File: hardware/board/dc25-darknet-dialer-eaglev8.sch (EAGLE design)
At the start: 86 parts, among them SW1 RESET, X1 10118193-0001LF, Y1 RESONATORSMD

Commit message: Updated silk screen parts indicators
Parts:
- renumbered SAMPLE_CAP_G1 to C23, SAMPLE_CAP_G2 to C24, SAMPLE_CAP_G3 to C22, SAMPLE_CAP_G5 to C25, U$11 to U2, U$19 to U1
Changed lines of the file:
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@@
 <part name="U$10" library="SYNShop" deviceset="VCC" device=""/>
 <part name="C16" library="darknet_parts_library" deviceset="C-US" device="C0603" value="4.7uF"/>
-<part name="U$11" library="darknet_parts_library" deviceset="DS21984E" device=""/>
+<part name="U2" library="darknet_parts_library" deviceset="DS21984E" device=""/>
 <part name="R22" library="darknet_parts_library" deviceset="RESISTOR" device="0603-RES"/>
 <part name="GND22" library="SYNShop" deviceset="GND" device=""/>
@@
 <part name="R28" library="darknet_parts_library" deviceset="RESISTOR" device="0603-RES" value="56"/>
 <part name="STLINK" library="darknet_parts_library" deviceset="STLINK-V2-CONNECTOR" device=""/>
-<part name="SAMPLE_CAP_G3" library="darknet_parts_library" deviceset="C-US" device="C0603" value="0.047uF"/>
-<part name="SAMPLE_CAP_G1" library="darknet_parts_library" deviceset="C-US" device="C0603" value="0.047uF"/>
-<part name="SAMPLE_CAP_G2" library="darknet_parts_library" deviceset="C-US" device="C0603" value="0.047uF"/>
-<part name="SAMPLE_CAP_G5" library="darknet_parts_library" deviceset="C-US" device="C0603" value="0.047uF"/>
+<part name="C22" library="darknet_parts_library" deviceset="C-US" device="C0603" value="0.047uF"/>
+<part name="C23" library="darknet_parts_library" deviceset="C-US" device="C0603" value="0.047uF"/>
+<part name="C24" library="darknet_parts_library" deviceset="C-US" device="C0603" value="0.047uF"/>
+<part name="C25" library="darknet_parts_library" deviceset="C-US" device="C0603" value="0.047uF"/>
 <part name="GND1" library="SYNShop" deviceset="GND" device=""/>
 <part name="GND11" library="SYNShop" deviceset="GND" device=""/>
@@
 <part name="U$14" library="SYNShop" deviceset="VCC" device=""/>
 <part name="GND14" library="SYNShop" deviceset="GND" device=""/>
-<part name="U$19" library="darknet_parts_library" deviceset="TLV702" device=""/>
+<part name="U1" library="darknet_parts_library" deviceset="TLV702" device=""/>
 <part name="GND15" library="SYNShop" deviceset="GND" device=""/>
 <part name="U$21" library="darknet_parts_library" deviceset="CHIP_ANTENNA" device=""/>
@@
 <instance part="U$10" gate="G$1" x="58.42" y="45.72"/>
 <instance part="C16" gate="G$1" x="17.78" y="40.64" rot="R180"/>
-<instance part="U$11" gate="G$1" x="106.68" y="294.64"/>
+<instance part="U2" gate="G$1" x="106.68" y="294.64"/>
 <instance part="R22" gate="G$1" x="121.92" y="289.56" rot="R90"/>
 <instance part="GND22" gate="1" x="121.92" y="279.4"/>
@@
 <instance part="R28" gate="G$1" x="246.38" y="76.2"/>
 <instance part="STLINK" gate="G$1" x="238.76" y="274.32"/>
-<instance part="SAMPLE_CAP_G3" gate="G$1" x="332.74" y="187.96" rot="R90"/>
-<instance part="SAMPLE_CAP_G1" gate="G$1" x="332.74" y="144.78" rot="R90"/>
-<instance part="SAMPLE_CAP_G2" gate="G$1" x="332.74" y="114.3" rot="R90"/>
-<instance part="SAMPLE_CAP_G5" gate="G$1" x="332.74" y="86.36" rot="R90"/>
+<instance part="C22" gate="G$1" x="332.74" y="187.96" rot="R90"/>
+<instance part="C23" gate="G$1" x="332.74" y="144.78" rot="R90"/>
+<instance part="C24" gate="G$1" x="332.74" y="114.3" rot="R90"/>
+<instance part="C25" gate="G$1" x="332.74" y="86.36" rot="R90"/>
 <instance part="GND1" gate="1" x="340.36" y="81.28"/>
 <instance part="GND11" gate="1" x="340.36" y="109.22"/>
@@
 <instance part="U$14" gate="G$1" x="264.16" y="274.32"/>
 <instance part="GND14" gate="1" x="264.16" y="256.54"/>
-<instance part="U$19" gate="G$1" x="101.6" y="391.16"/>
+<instance part="U1" gate="G$1" x="101.6" y="391.16"/>
 <instance part="GND15" gate="1" x="101.6" y="373.38"/>
 <instance part="U$21" gate="G$1" x="177.8" y="170.18"/>
@@
 </segment>
 <segment>
-<pinref part="U$11" gate="G$1" pin="VSS"/>
+<pinref part="U2" gate="G$1" pin="VSS"/>
 <pinref part="R22" gate="G$1" pin="1"/>
 <wire x1="119.38" y1="284.48" x2="121.92" y2="284.48" width="0.1524" layer="91"/>
@@
 </segment>
 <segment>
-<pinref part="SAMPLE_CAP_G1" gate="G$1" pin="2"/>
+<pinref part="C23" gate="G$1" pin="2"/>
 <pinref part="GND12" gate="1" pin="GND"/>
 <wire x1="337.82" y1="144.78" x2="340.36" y2="144.78" width="0.1524" layer="91"/>
@@
 </segment>
 <segment>
-<pinref part="SAMPLE_CAP_G2" gate="G$1" pin="2"/>
+<pinref part="C24" gate="G$1" pin="2"/>
 <pinref part="GND11" gate="1" pin="GND"/>
 <wire x1="337.82" y1="114.3" x2="340.36" y2="114.3" width="0.1524" layer="91"/>
@@
 </segment>
 <segment>
-<pinref part="SAMPLE_CAP_G5" gate="G$1" pin="2"/>
+<pinref part="C25" gate="G$1" pin="2"/>
 <pinref part="GND1" gate="1" pin="GND"/>
 <wire x1="337.82" y1="86.36" x2="340.36" y2="86.36" width="0.1524" layer="91"/>
@@
 </segment>
 <segment>
-<pinref part="SAMPLE_CAP_G3" gate="G$1" pin="2"/>
+<pinref part="C22" gate="G$1" pin="2"/>
 <pinref part="GND13" gate="1" pin="GND"/>
 <wire x1="337.82" y1="187.96" x2="340.36" y2="187.96" width="0.1524" layer="91"/>
@@
 <segment>
 <pinref part="GND15" gate="1" pin="GND"/>
-<pinref part="U$19" gate="G$1" pin="GND"/>
+<pinref part="U1" gate="G$1" pin="GND"/>
 <wire x1="101.6" y1="375.92" x2="101.6" y2="378.46" width="0.1524" layer="91"/>
 <pinref part="C21" gate="G$1" pin="1"/>
@@
 </segment>
 <segment>
-<pinref part="SAMPLE_CAP_G1" gate="G$1" pin="1"/>
+<pinref part="C23" gate="G$1" pin="1"/>
 <wire x1="330.2" y1="144.78" x2="297.18" y2="144.78" width="0.1524" layer="91"/>
 <label x="294.64" y="144.78" size="1.778" layer="95" rot="MR0"/>
@@
 <segment>
 <label x="294.64" y="187.96" size="1.778" layer="95" rot="R180"/>
-<pinref part="SAMPLE_CAP_G3" gate="G$1" pin="1"/>
+<pinref part="C22" gate="G$1" pin="1"/>
 <wire x1="330.2" y1="187.96" x2="297.18" y2="187.96" width="0.1524" layer="91"/>
 </segment>
@@
 <wire x1="134.62" y1="396.24" x2="134.62" y2="401.32" width="0.1524" layer="91"/>
 <pinref part="U$13" gate="G$1" pin="VCC"/>
-<pinref part="U$19" gate="G$1" pin="VOUT"/>
+<pinref part="U1" gate="G$1" pin="VOUT"/>
 <wire x1="116.84" y1="396.24" x2="124.46" y2="396.24" width="0.1524" layer="91"/>
 <wire x1="124.46" y1="396.24" x2="124.46" y2="393.7" width="0.1524" layer="91"/>
@@
 </segment>
 <segment>
-<pinref part="SAMPLE_CAP_G5" gate="G$1" pin="1"/>
+<pinref part="C25" gate="G$1" pin="1"/>
 <wire x1="330.2" y1="86.36" x2="297.18" y2="86.36" width="0.1524" layer="91"/>
 <label x="294.64" y="86.36" size="1.778" layer="95" rot="MR0"/>
@@
 <net name="N$22" class="0">
 <segment>
-<pinref part="U$11" gate="G$1" pin="PROG"/>
+<pinref part="U2" gate="G$1" pin="PROG"/>
 <pinref part="R22" gate="G$1" pin="2"/>
 <wire x1="119.38" y1="294.64" x2="121.92" y2="294.64" width="0.1524" layer="91"/>
@@
 <pinref part="LED11" gate="G$1" pin="C"/>
 <wire x1="86.36" y1="287.02" x2="86.36" y2="284.48" width="0.1524" layer="91"/>
-<pinref part="U$11" gate="G$1" pin="STAT"/>
+<pinref part="U2" gate="G$1" pin="STAT"/>
 <wire x1="86.36" y1="284.48" x2="91.44" y2="284.48" width="0.1524" layer="91"/>
 </segment>
@@
 <net name="VCC0" class="0">
 <segment>
-<pinref part="U$11" gate="G$1" pin="VDD"/>
+<pinref part="U2" gate="G$1" pin="VDD"/>
 <pinref part="R23" gate="G$1" pin="2"/>
 <wire x1="91.44" y1="304.8" x2="86.36" y2="304.8" width="0.1524" layer="91"/>
@@
 <net name="VCC1" class="0">
 <segment>
-<pinref part="U$11" gate="G$1" pin="VBAT"/>
+<pinref part="U2" gate="G$1" pin="VBAT"/>
 <wire x1="119.38" y1="304.8" x2="129.54" y2="304.8" width="0.1524" layer="91"/>
 <pinref part="C17" gate="G$1" pin="2"/>
@@
 </segment>
 <segment>
-<pinref part="SAMPLE_CAP_G2" gate="G$1" pin="1"/>
+<pinref part="C24" gate="G$1" pin="1"/>
 <wire x1="330.2" y1="114.3" x2="297.18" y2="114.3" width="0.1524" layer="91"/>
 <label x="294.64" y="114.3" size="1.778" layer="95" rot="MR0"/>
@@
 <segment>
 <pinref part="F1" gate="G$1" pin="2"/>
-<pinref part="U$19" gate="G$1" pin="VIN"/>
+<pinref part="U1" gate="G$1" pin="VIN"/>
 <wire x1="81.28" y1="396.24" x2="83.82" y2="396.24" width="0.1524" layer="91"/>
-<pinref part="U$19" gate="G$1" pin="EN"/>
+<pinref part="U1" gate="G$1" pin="EN"/>
 <wire x1="83.82" y1="396.24" x2="86.36" y2="396.24" width="0.1524" layer="91"/>
 <wire x1="86.36" y1="386.08" x2="83.82" y2="386.08" width="0.1524" layer="91"/>

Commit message: Updated parts for upload to MacroFab
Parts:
- C1: value 0.5pF -> 251R14S0R5BV4T
- C16: value 4.7uF -> GRM188R61A475ME15D
- C17: value 1uF -> GRM188R61A475ME15D
- C18: value (none) -> GRM188R61A475ME15D
- C19, C20: value 47pF -> C0603C470J3GACTU
- C22, C23, C24, C25: value 0.047uF -> C0603C473J3RACAUTO
- F1: value 500uA -> 0ZCA0050FF2G
- L1: value (none) -> BLM21PG221SN1D
- L2: value 10nH -> CI160808-10NJ
- L3: value 4.7nH -> CI160808-4N7D
- LED11: device SYNShop:LED0603 -> SYNShop:LED5MM
- LED12: value (none) -> MF-LED-0603-GREEN; device SYNShop:LED5MM -> SYNShop:LED0603
- LED13: value (none) -> MF-LED-0603-GREEN
- R1, R10, R2, R3, R4, R5, R6, R7, R8, R9: value 47 -> CRCW120647R0JNEA
- R22: value (none) -> 2K
- R23: value (none) -> 470
- R24: value 56 -> 47
- R25: value (none) -> 10K
- R28: value 56 -> 68
- U$2: value STM32F302XC -> STM32F302RBT6
- U$21: value CHIP_ANTENNA -> 0915AT43A0026E
- U1: value TLV702 -> BU33SD5WG-TR
- U2: value DS21984E -> MCP73831T-5ACI/OT
- Y1: value RESONATORSMD -> CSTCE8M00G52-R0
- renumbered U$17 to U3
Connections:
- net N$23: now also LED11.A; no longer LED12.A
- net N$24: now also LED12.A; no longer LED11.A
- net N$25: now also LED12.C; no longer LED11.C
- net TIM_IR_CARRIER_FREQ: now also LED11.C; no longer LED12.C
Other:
- note added: "0.047uF"
- note added: "0.5pF"
- note added: "10nH"
- note added: "4.7nH"
- note added: "4.7uF"
- note added: "47pF"
- note added: "Ferrite Bead"
- note added: "PTC 0.5A Resettable Fuse"
- note removed: "3.3V LDO Voltage regulator Here.. need to make part"
- moved on the sheet: LED11, LED12

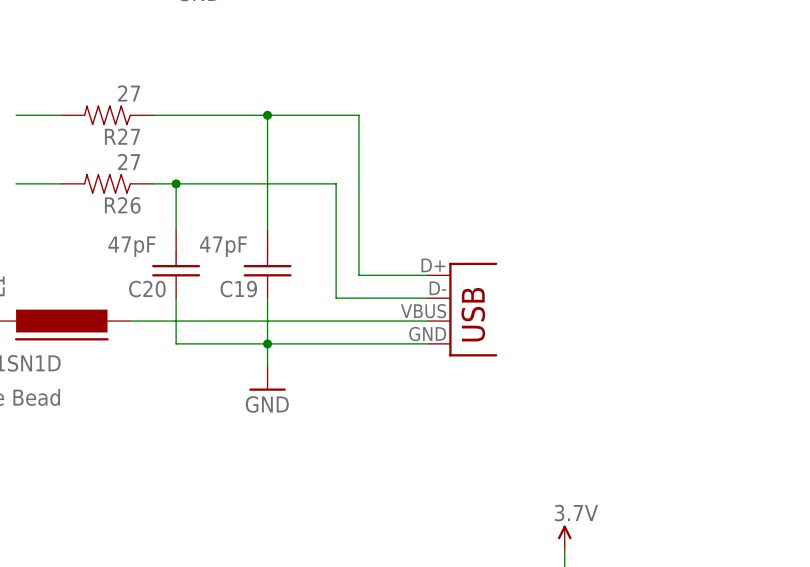
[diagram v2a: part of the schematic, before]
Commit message: Changed USB connector to Macrofab eagle library
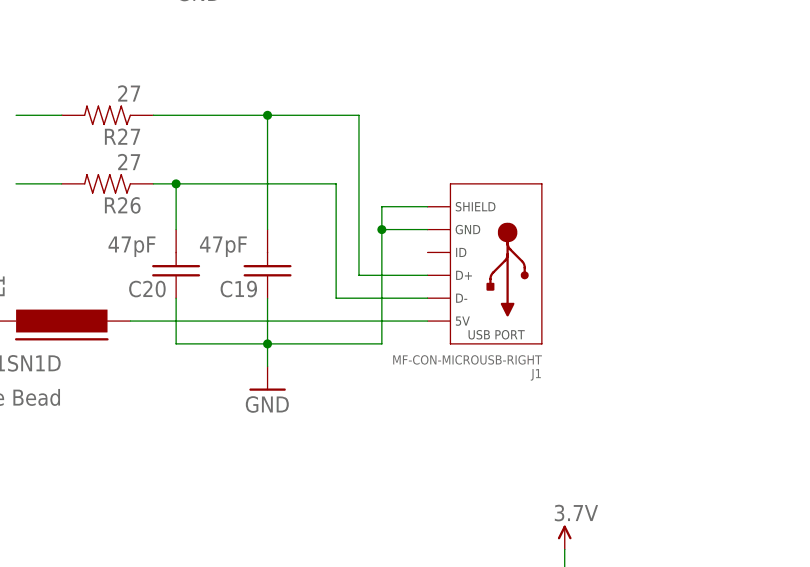
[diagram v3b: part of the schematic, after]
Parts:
- removed X1: 10118193-0001LF, SYNShop:USB-MICROB
- added J1: MF-CON-MICROUSB-RIGHT, MF_Connectors:USB_MICRO_RIGHT
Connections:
- net GND: now also J1.GND, J1.SLD; no longer X1.GND
- net N$26: now also J1.D+; no longer X1.D+
- net N$27: now also J1.D-; no longer X1.D-
- net N$28: now also J1.5V; no longer X1.VBUS

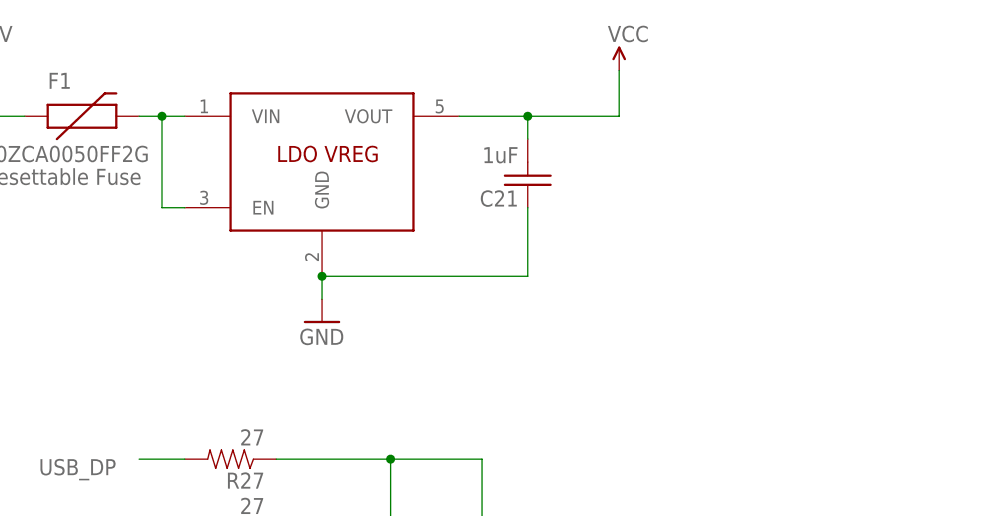
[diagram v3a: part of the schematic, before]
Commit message: Added on/off switch
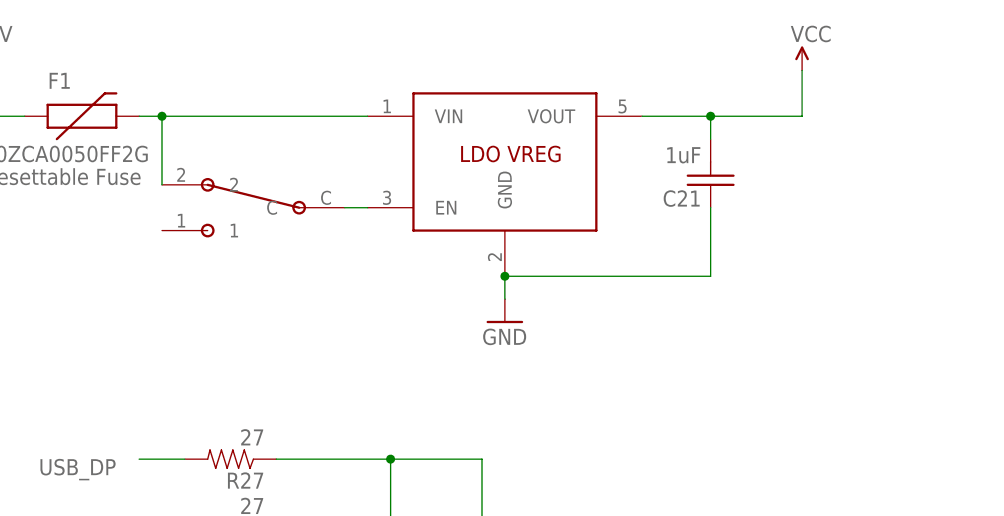
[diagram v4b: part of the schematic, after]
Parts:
- added U$11: SWITCH_SPDT, darknet_parts_library:SWITCH_SPDT
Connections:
- new net N$32: U$11.C, U1.EN
- net N$30: now also U$11.2; no longer U1.EN
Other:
- moved on the sheet: C21
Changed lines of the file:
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@@
 <part name="U$23" library="darknet_parts_library" deviceset="CMD_C0DE_LOGO" device=""/>
 <part name="J1" library="MF_Connectors" deviceset="USB" device="_MICRO_RIGHT" value="MF-CON-MICROUSB-RIGHT"/>
+<part name="U$11" library="darknet_parts_library" deviceset="SWITCH_SPDT" device=""/>
 </parts>
 <sheets>
@@
 </instance>
 <instance part="3.7V1" gate="G$1" x="63.5" y="401.32"/>
-<instance part="C21" gate="G$1" x="124.46" y="388.62" rot="R180"/>
-<instance part="U$13" gate="G$1" x="134.62" y="401.32"/>
+<instance part="C21" gate="G$1" x="144.78" y="388.62" rot="R180"/>
+<instance part="U$13" gate="G$1" x="154.94" y="401.32"/>
 <instance part="LED13" gate="G$1" x="254" y="76.2" rot="R90"/>
 <instance part="R28" gate="G$1" x="246.38" y="76.2"/>
@@
 <instance part="U$14" gate="G$1" x="264.16" y="274.32"/>
 <instance part="GND14" gate="1" x="264.16" y="256.54"/>
-<instance part="U1" gate="G$1" x="101.6" y="391.16"/>
-<instance part="GND15" gate="1" x="101.6" y="373.38"/>
+<instance part="U1" gate="G$1" x="121.92" y="391.16"/>
+<instance part="GND15" gate="1" x="121.92" y="373.38"/>
 <instance part="U$21" gate="G$1" x="177.8" y="170.18"/>
 <instance part="C1" gate="G$1" x="162.56" y="157.48" smashed="yes" rot="R180">
@@
 <instance part="U$23" gate="G$1" x="33.02" y="5.08"/>
 <instance part="J1" gate="G$1" x="134.62" y="340.36" rot="R180"/>
+<instance part="U$11" gate="G$1" x="93.98" y="386.08"/>
 </instances>
 <busses>
@@
 <pinref part="GND15" gate="1" pin="GND"/>
 <pinref part="U1" gate="G$1" pin="GND"/>
-<wire x1="101.6" y1="375.92" x2="101.6" y2="378.46" width="0.1524" layer="91"/>
+<wire x1="121.92" y1="375.92" x2="121.92" y2="378.46" width="0.1524" layer="91"/>
 <pinref part="C21" gate="G$1" pin="1"/>
-<wire x1="101.6" y1="378.46" x2="124.46" y2="378.46" width="0.1524" layer="91"/>
-<wire x1="124.46" y1="378.46" x2="124.46" y2="386.08" width="0.1524" layer="91"/>
-<junction x="101.6" y="378.46"/>
+<wire x1="121.92" y1="378.46" x2="144.78" y2="378.46" width="0.1524" layer="91"/>
+<wire x1="144.78" y1="378.46" x2="144.78" y2="386.08" width="0.1524" layer="91"/>
+<junction x="121.92" y="378.46"/>
 </segment>
 <segment>
@@
 <segment>
 <pinref part="C21" gate="G$1" pin="2"/>
-<wire x1="124.46" y1="396.24" x2="134.62" y2="396.24" width="0.1524" layer="91"/>
-<wire x1="134.62" y1="396.24" x2="134.62" y2="401.32" width="0.1524" layer="91"/>
+<wire x1="144.78" y1="396.24" x2="154.94" y2="396.24" width="0.1524" layer="91"/>
+<wire x1="154.94" y1="396.24" x2="154.94" y2="401.32" width="0.1524" layer="91"/>
 <pinref part="U$13" gate="G$1" pin="VCC"/>
 <pinref part="U1" gate="G$1" pin="VOUT"/>
-<wire x1="116.84" y1="396.24" x2="124.46" y2="396.24" width="0.1524" layer="91"/>
-<wire x1="124.46" y1="396.24" x2="124.46" y2="393.7" width="0.1524" layer="91"/>
-<junction x="124.46" y="396.24"/>
+<wire x1="137.16" y1="396.24" x2="144.78" y2="396.24" width="0.1524" layer="91"/>
+<wire x1="144.78" y1="396.24" x2="144.78" y2="393.7" width="0.1524" layer="91"/>
+<junction x="144.78" y="396.24"/>
 </segment>
 <segment>
@@
 <pinref part="U1" gate="G$1" pin="VIN"/>
 <wire x1="81.28" y1="396.24" x2="83.82" y2="396.24" width="0.1524" layer="91"/>
-<pinref part="U1" gate="G$1" pin="EN"/>
-<wire x1="83.82" y1="396.24" x2="86.36" y2="396.24" width="0.1524" layer="91"/>
-<wire x1="86.36" y1="386.08" x2="83.82" y2="386.08" width="0.1524" layer="91"/>
-<wire x1="83.82" y1="386.08" x2="83.82" y2="396.24" width="0.1524" layer="91"/>
+<pinref part="U$11" gate="G$1" pin="2"/>
+<wire x1="83.82" y1="396.24" x2="106.68" y2="396.24" width="0.1524" layer="91"/>
+<wire x1="83.82" y1="388.62" x2="83.82" y2="396.24" width="0.1524" layer="91"/>
 <junction x="83.82" y="396.24"/>
 </segment>
@@
 </segment>
 </net>
+<net name="N$32" class="0">
+<segment>
+<pinref part="U1" gate="G$1" pin="EN"/>
+<pinref part="U$11" gate="G$1" pin="C"/>
+<wire x1="106.68" y1="386.08" x2="104.14" y2="386.08" width="0.1524" layer="91"/>
+</segment>
+</net>
